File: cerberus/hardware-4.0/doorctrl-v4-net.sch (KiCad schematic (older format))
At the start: 1 part, among them U4 ENC28J60

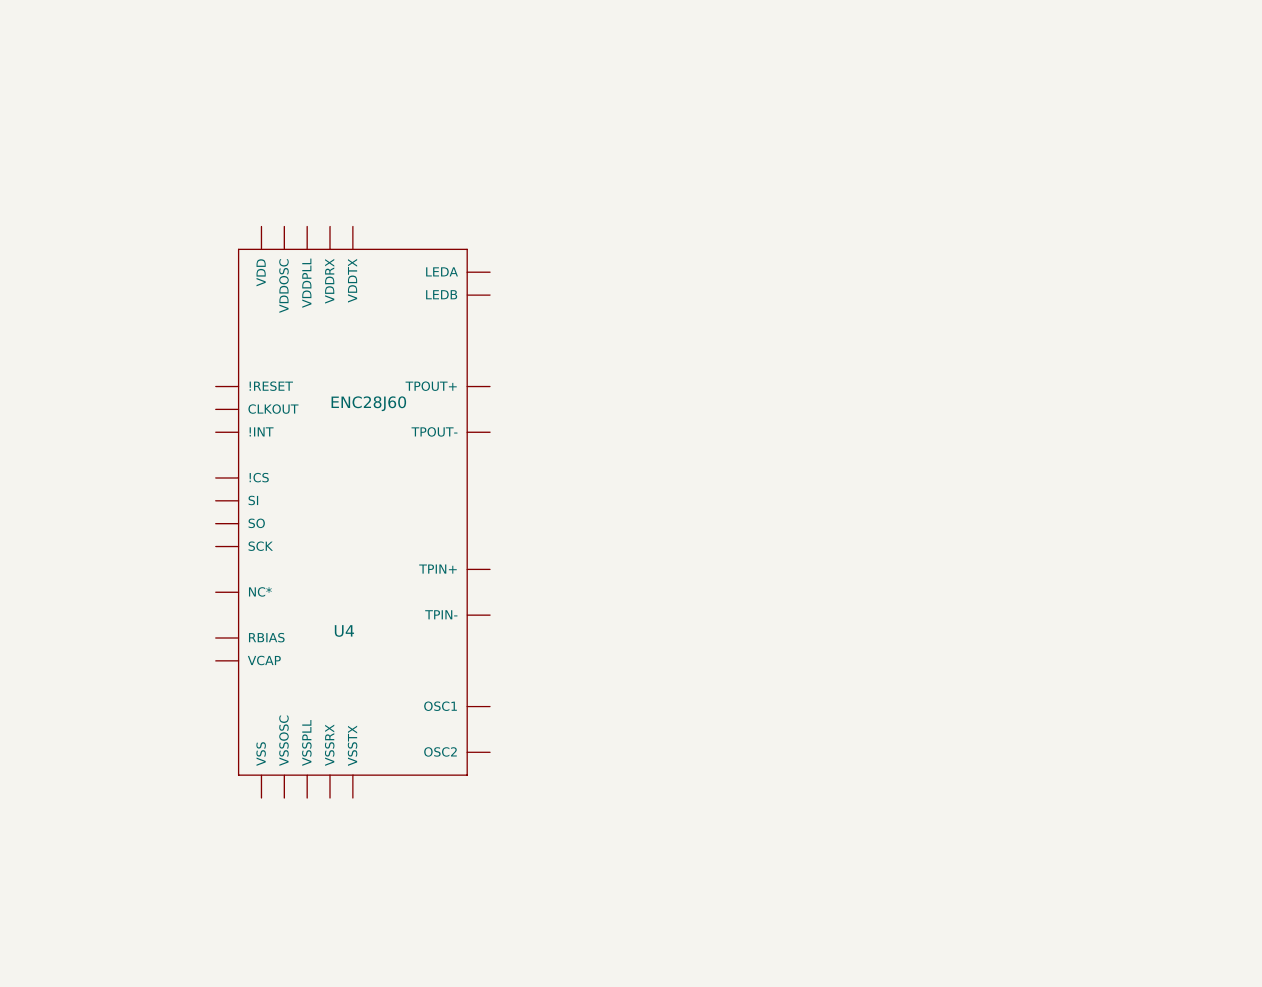
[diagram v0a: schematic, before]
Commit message: Added ENC28J60 and friends
git-svn-id: file:///home/ff/projects/osaa/svn@214 a092026d-3e22-4cff-94a7-eaa6fdd35d37
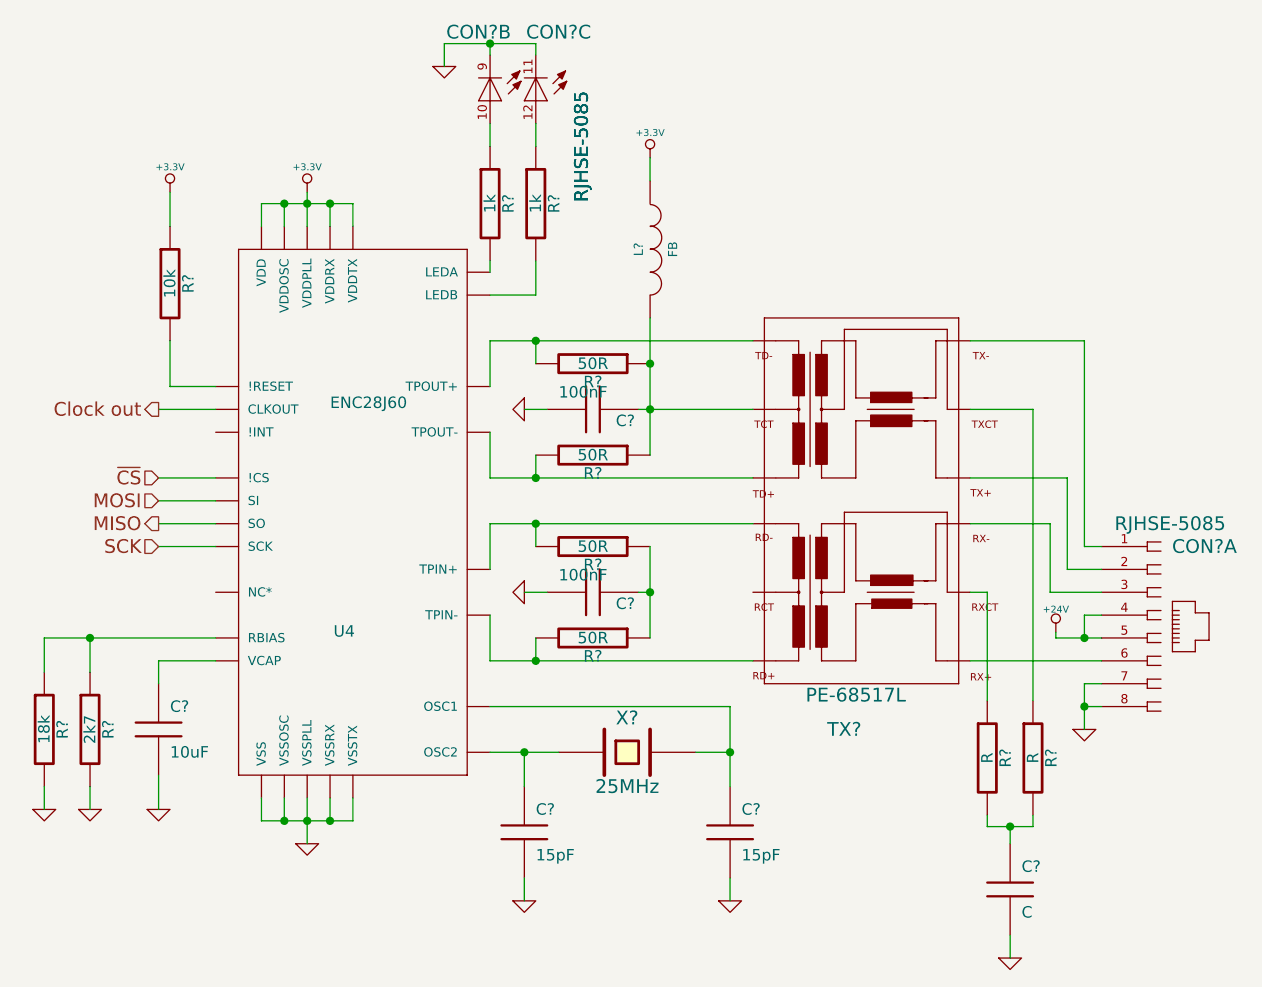
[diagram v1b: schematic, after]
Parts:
- added C?: 10uF, symbol C
- added C? (x2): 15pF, symbol C
- added C? (x2): 100nF, symbol C
- added C?: C, symbol C
- added CON? (x3): RJHSE-5085, symbol RJHSE-5085
- added L?: FB, symbol INDUCTOR
- added R? (x2): 1k, symbol R
- added R?: 2k7, symbol R
- added R?: 18k, symbol R
- added R?: 10k, symbol R
- added R? (x4): 50R, symbol R
- added R? (x2): R, symbol R
- added TX?: PE-68517L, symbol PE-68517L
- added X?: 25MHz, symbol CRYSTAL
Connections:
- net at U4.1 (VCAP): now also C?.1
- net at U4.10 (!RESET): now also R?.2
- net GND: now reaches U4.11 (VSSRX)
- net GND: now also U4.18 (VSSTX), U4.2 (VSS), U4.21 (VSSPLL), U4.22 (VSSOSC), C?.2, C?.2, C?.2, C?.2, C?.2, C?.2, CON?.11 (C), CON?.7, CON?.8, CON?.9 (C), R?.2, R?.2
- net at U4.12 (TPIN-): now also R?.2, TX?.16 (RD+)
- net at U4.13 (TPIN+): now also R?.2, TX?.15 (RD-)
- net at U4.14 (RBIAS): now also R?.1, R?.1
- net +3.3V: now reaches U4.15 (VDDTX)
- net +3.3V: now also U4.19 (VDDRX), U4.20 (VDDPLL), U4.25 (VDDOSC), U4.28 (VDD), L?.1, R?.1
- net at U4.16 (TPOUT-): now also R?.2, TX?.1 (TD+)
- net at U4.17 (TPOUT+): now also R?.2, TX?.2 (TD-)
- net at U4.23 (OSC1): now also C?.1, X?.2
- net at U4.24 (OSC2): now also C?.1, X?.1
- net at U4.26 (LEDB): now also R?.2
- net at U4.27 (LEDA): now also R?.2
- net Clock out: now reaches U4.3 (CLKOUT)
- net MISO: now reaches U4.6 (SO)
- net MOSI: now reaches U4.7 (SI)
- net SCK: now reaches U4.8 (SCK)
- net ~CS: now reaches U4.9 (!CS)
- new net: CON?.1, TX?.7 (TX-)
- new net: CON?.2, TX?.8 (TX+)
- new net: CON?.3, TX?.10 (RX-)
- new net: CON?.6, TX?.9 (RX+)
- new net: CON?.12 (A), R?.1
- new net: CON?.10 (A), R?.1
- new net: R?.1, TX?.11 (RXCT)
- new net: C?.1, L?.2, R?.1, R?.1, TX?.3 (TCT)
- new net: R?.1, TX?.6 (TXCT)
- new net: C?.1, R?.1, R?.1
- new net: C?.1, R?.2, R?.2
- new net +24V: CON?.4, CON?.5

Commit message: Added ENC28J60 and friends
git-svn-id: file:///home/ff/projects/osaa/svn@215 a092026d-3e22-4cff-94a7-eaa6fdd35d37
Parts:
- C?: value C -> 1nF
- R? (x2): value R -> 75R
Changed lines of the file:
@@
-EESchema Schematic File Version 2  date 2010-12-15T21:22:19 CET
+EESchema Schematic File Version 2  date 2010-12-15T21:23:41 CET
 LIBS:enc28j60
 LIBS:power
@@
 P 6075 4550
 F 0 "C?" H 6125 4650 50  0000 L CNN
-F 1 "C" H 6125 4450 50  0000 L CNN
+F 1 "1nF" H 6125 4450 50  0000 L CNN
 	1    6075 4550
 	1    0    0    -1
@@
 P 6175 3975
 F 0 "R?" V 6255 3975 50  0000 C CNN
-F 1 "R" V 6175 3975 50  0000 C CNN
+F 1 "75R" V 6175 3975 50  0000 C CNN
 	1    6175 3975
 	1    0    0    -1
@@
 P 5975 3975
 F 0 "R?" V 6055 3975 50  0000 C CNN
-F 1 "R" V 5975 3975 50  0000 C CNN
+F 1 "75R" V 5975 3975 50  0000 C CNN
 	1    5975 3975
 	1    0    0    -1

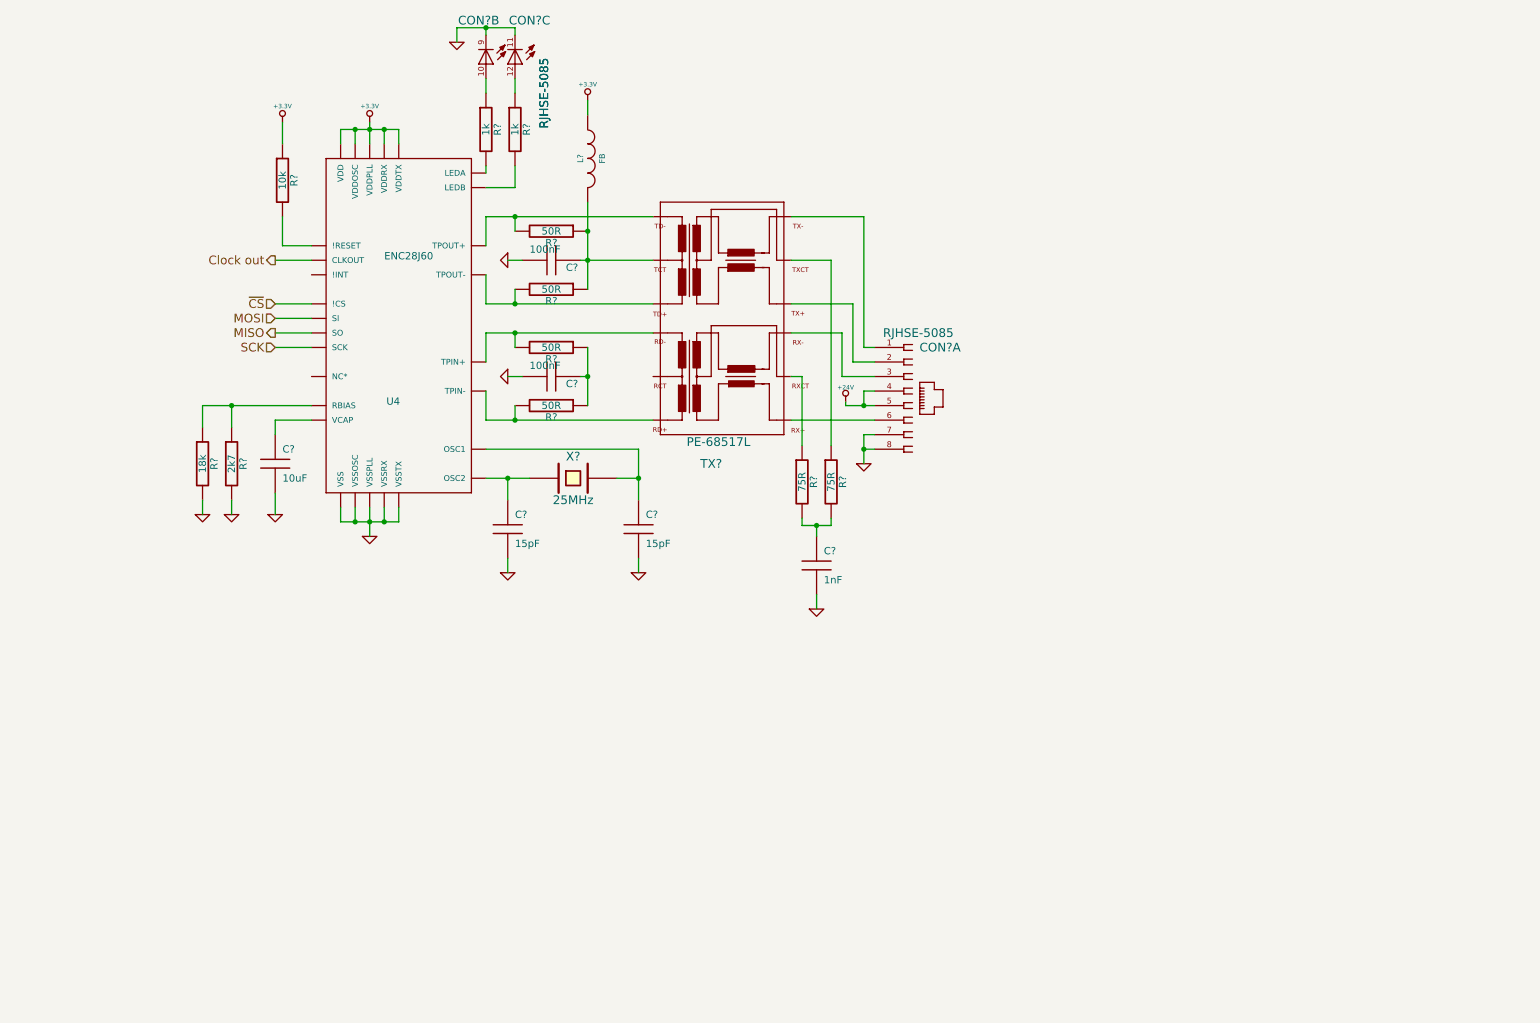
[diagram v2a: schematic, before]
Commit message: Added RS-485 transciever and connectors
git-svn-id: file:///home/ff/projects/osaa/svn@216 a092026d-3e22-4cff-94a7-eaa6fdd35d37
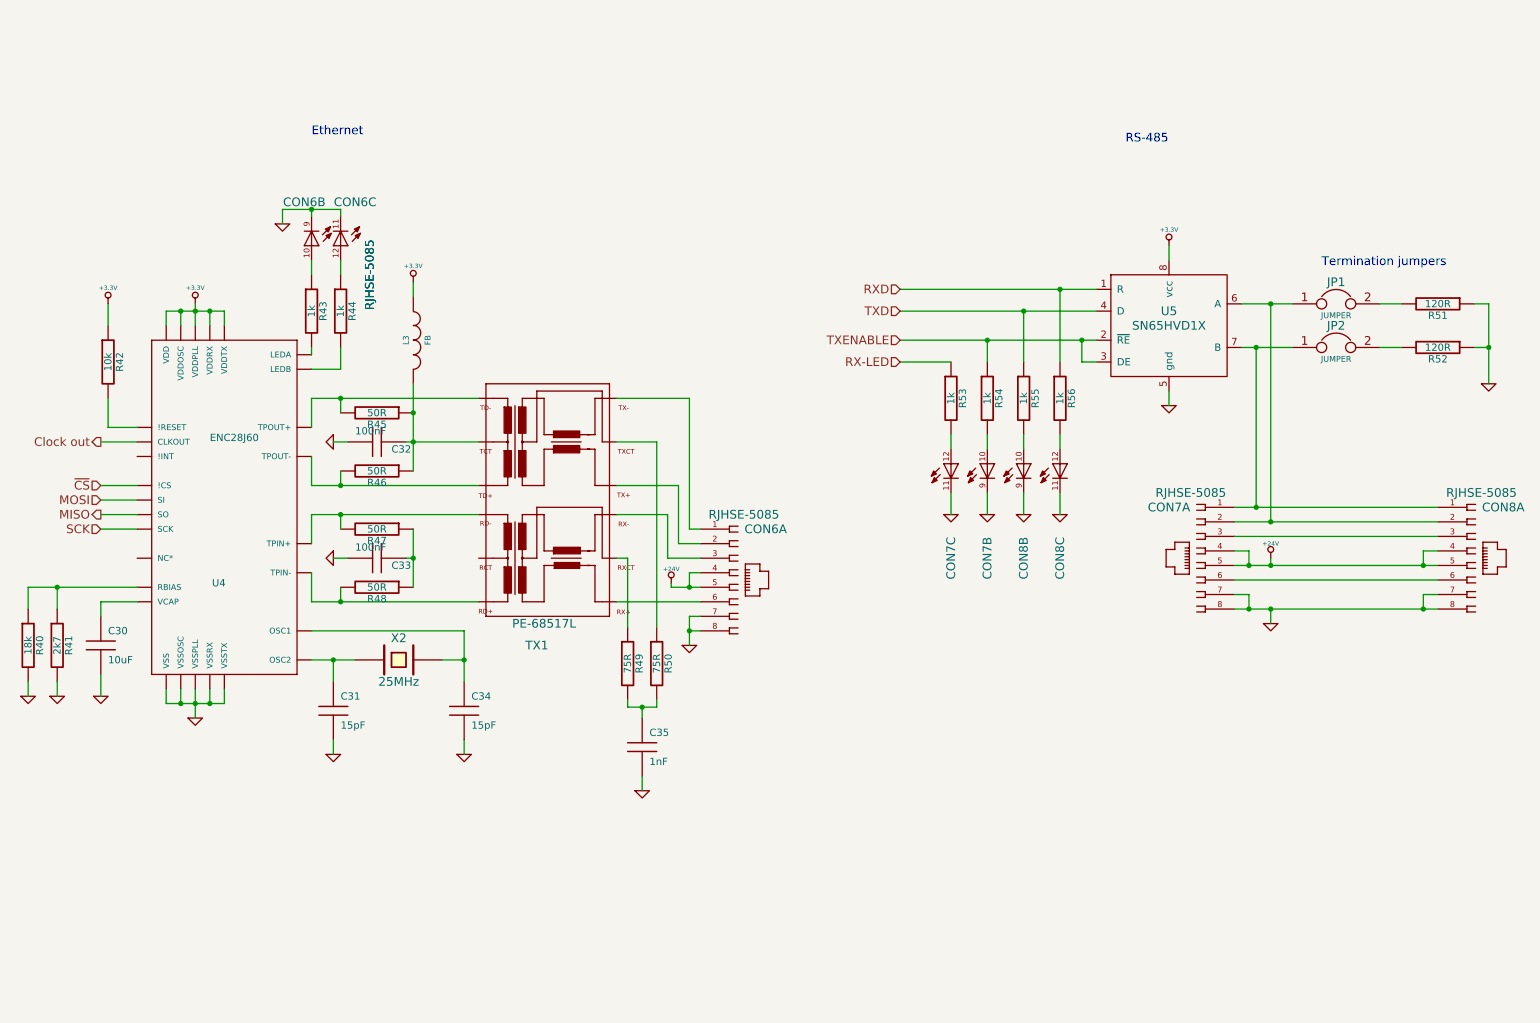
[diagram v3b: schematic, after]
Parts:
- added CON7, CON8: RJHSE-5085, symbol RJHSE-5085
- added JP1, JP2: JUMPER, symbol JUMPER
- added R51, R52: 120R, symbol R
- added R53, R54, R55, R56: 1k, symbol R
- added U5: SN65HVD1X, so8, symbol SN65HVD1X
- gave numbers to parts that had none: 21
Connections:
- net +24V: now also CON7.4, CON7.5, CON8.4, CON8.5
- net +3.3V: now also U5.8 (vcc)
- net GND: now also CON7.11 (C), CON7.7, CON7.8, CON7.9 (C), CON8.11 (C), CON8.7, CON8.8, CON8.9 (C), R51.1, R52.1, U5.5 (gnd)
- new net: CON7.2, CON8.2, JP1.1, U5.6 (A)
- new net: CON7.1, CON8.1, JP2.1, U5.7 (B)
- new net: CON7.3, CON8.3
- new net: CON7.6, CON8.6
- new net: CON7.10 (A), R54.2
- new net: CON7.12 (A), R53.2
- new net: CON8.10 (A), R55.2
- new net: CON8.12 (A), R56.2
- new net: JP1.2, R51.2
- new net: JP2.2, R52.2
- new net RX-LED: R53.1
- new net RXD: R56.1, U5.1 (R)
- new net TXD: R55.1, U5.4 (D)
- new net TXENABLE: R54.1, U5.2 (~RE), U5.3 (DE)
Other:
- note added: "Ethernet"
- note added: "RS-485"
- note added: "Termination jumpers"
- moved on the sheet: C30, C31, C32, C33, C34, C35, CON6A, CON6B, CON6C, L3, R40, R41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

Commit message: Added a 5V regulator for most stuff, except ENC28J60 which lives on its own 3.3v supply
git-svn-id: file:///home/ff/projects/osaa/svn@217 a092026d-3e22-4cff-94a7-eaa6fdd35d37
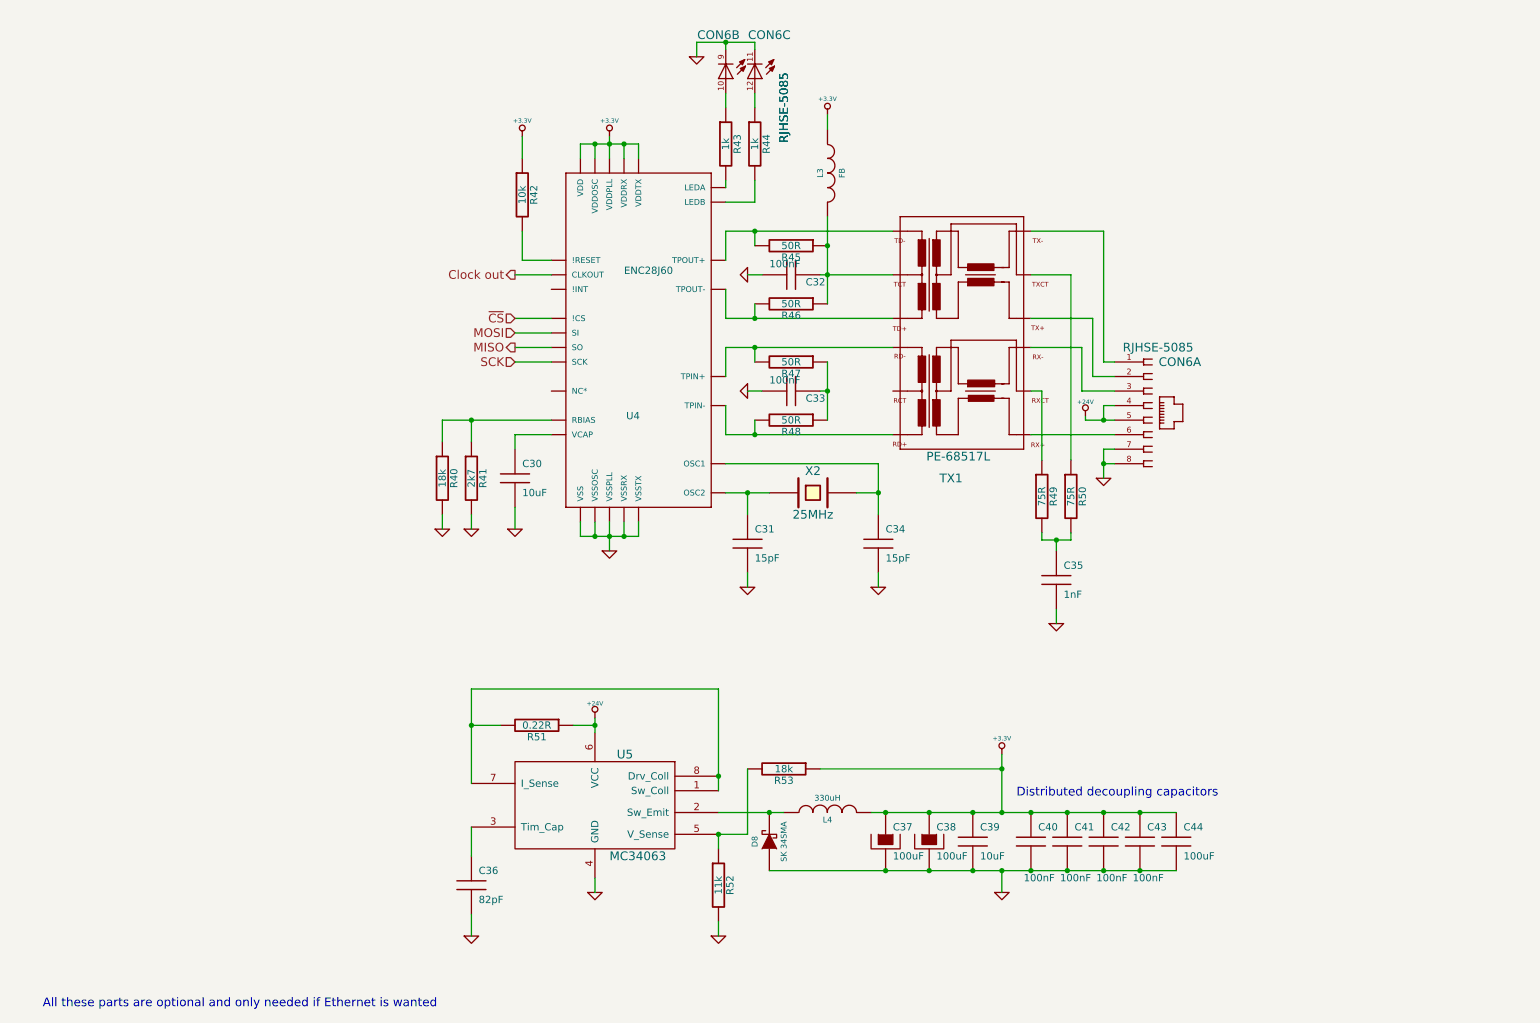
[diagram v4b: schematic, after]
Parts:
- removed CON7, CON8: RJHSE-5085, symbol RJHSE-5085
- removed JP1, JP2: JUMPER, symbol JUMPER
- removed R54, R55, R56: 1k, symbol R
- removed U5: SN65HVD1X, so8, symbol SN65HVD1X
- added C36: 82pF, symbol C
- added C37, C38: 100uF, symbol CAPAPOL
- added C39: 10uF, symbol C
- added C40, C41, C42, C43: 100nF, symbol C
- added C44: 100uF, symbol C
- added D8: SK 34SMA, symbol DIODESCH
- added L4: 330uH, symbol INDUCTOR
- added U5: MC34063, symbol MC34063
- R51: value 120R -> 0.22R
- R52: value 120R -> 11k
- R53: value 1k -> 18k
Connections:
- net RX-LED is gone; now on net +3.3V: R53.1
- net +24V: now also R51.1, U5.6 (VCC)
- net +3.3V: now also C37.1, C38.1, C39.1, C40.1, C41.1, C42.1, C43.1, C44.1, L4.2
- net GND: now also R52.2, C36.2, C37.2, C38.2, C39.2, C40.2, C41.2, C42.2, C43.2, C44.2, D8.1 (A), U5.4 (GND); no longer R51.1, R52.1
- net at R53.2: now also R52.1, U5.5 (V_Sense)
- net at R51.2: now also U5.1 (Sw_Coll), U5.7 (I_Sense), U5.8 (Drv_Coll)
- new net: D8.2 (K), L4.1, U5.2 (Sw_Emit)
- new net: C36.1, U5.3 (Tim_Cap)
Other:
- note added: "All these parts are optional and only needed if Ethernet is wanted"
- note added: "Distributed decoupling capacitors"
- note removed: "Ethernet"
- note removed: "RS-485"
- note removed: "Termination jumpers"
- moved on the sheet: C30, C31, C32, C33, C34, C35, CON6A, CON6B, CON6C, L3, R40, R41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
